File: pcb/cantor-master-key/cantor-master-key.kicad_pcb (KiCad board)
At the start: 2 copper layers, 142.9 x 98.6 mm, 26 parts, among them J1 TRRS, K00 KEYSW, K01 KEYSW, K02 KEYSW, K03 KEYSW, K04 KEYSW, K05 KEYSW, K10 KEYSW, K11 KEYSW, K12 KEYSW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

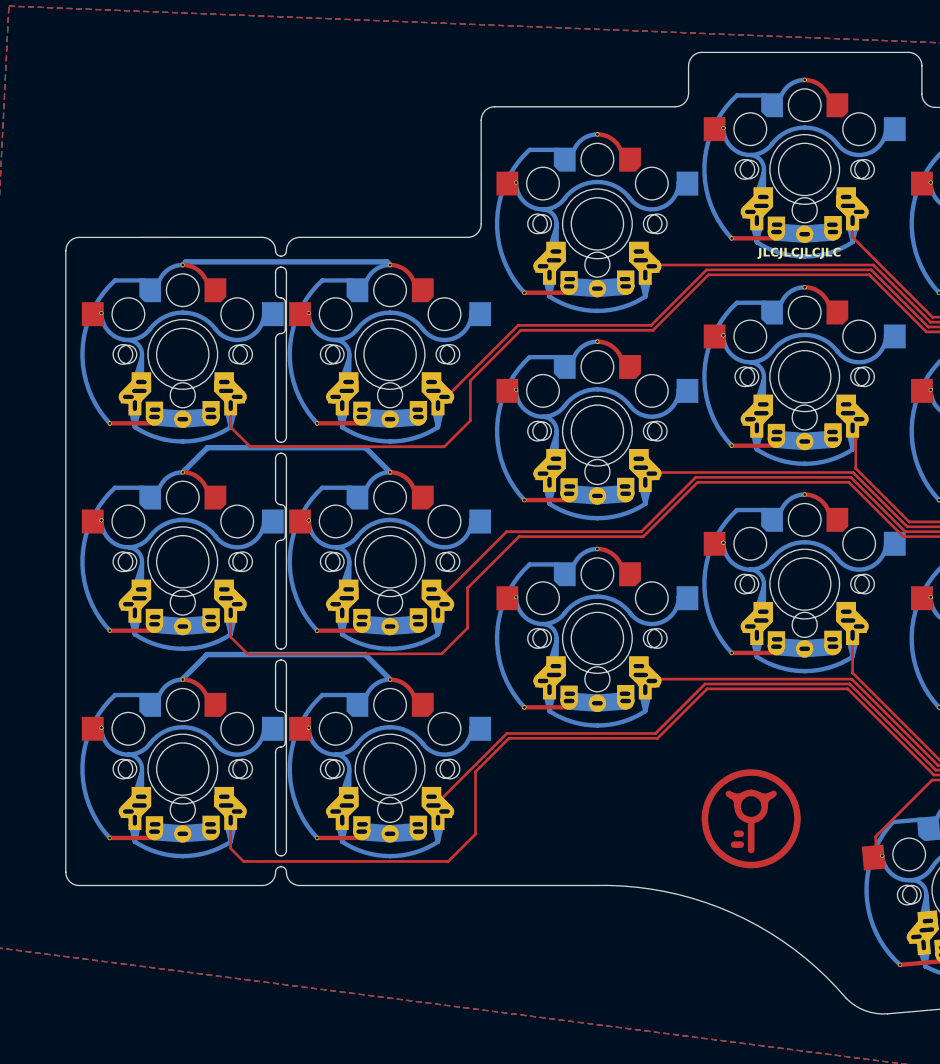
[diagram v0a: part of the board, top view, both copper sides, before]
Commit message: Made truncated version for footprint prototype
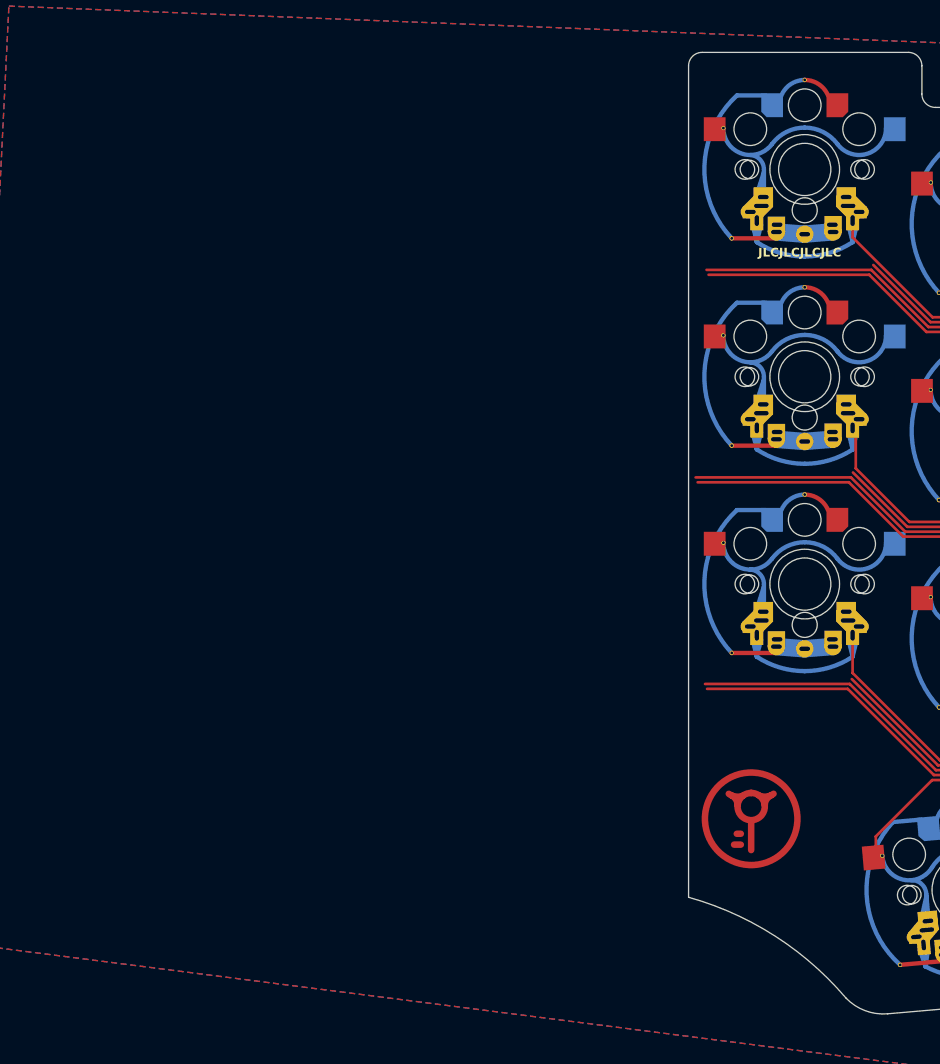
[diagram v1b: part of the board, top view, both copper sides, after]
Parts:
- removed K00, K01, K02, K10, K11, K12, K20, K21, K22: KEYSW, Cantor_MasterKey:ALL LOWs CANTOR v4.1
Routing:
- net GND: track 122.0 -> 60.9 mm
- net /k20: track 170.9 -> 114.1 mm
- net /k00: track 170.2 -> 114.9 mm
- net /k10: track 140.2 -> 85.8 mm
- net /k21: track 145.9 -> 116.2 mm
- net /k01: track 118.2 -> 89.3 mm
- net /k11: track 113.6 -> 85.3 mm
- net /k02: track 105.1 -> 82.6 mm
- net /k22: track 125.0 -> 105.9 mm
- net /k12: track 92.0 -> 73.5 mm
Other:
- board size 142.9 x 98.6 mm -> 85.6 x 98.6 mm
